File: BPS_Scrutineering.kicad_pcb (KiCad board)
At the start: 2 copper layers, 89 x 172 mm, 158 parts, among them J1 Conn_01x09, J10 BottomConn, J2 Conn_01x09, J3 Conn_01x09, J4 Conn_01x09, J5 TopConn, J6 BottomConn, J7 TopConn, J8 BottomConn, J9 TopConn, SW1 SW_DIP_x07, SW2 SW_DIP_x07, SW3 SW_DIP_x07, SW4 SW_DIP_x07, SW5 SW_DIP_x07, SW6 SW_DIP_x07

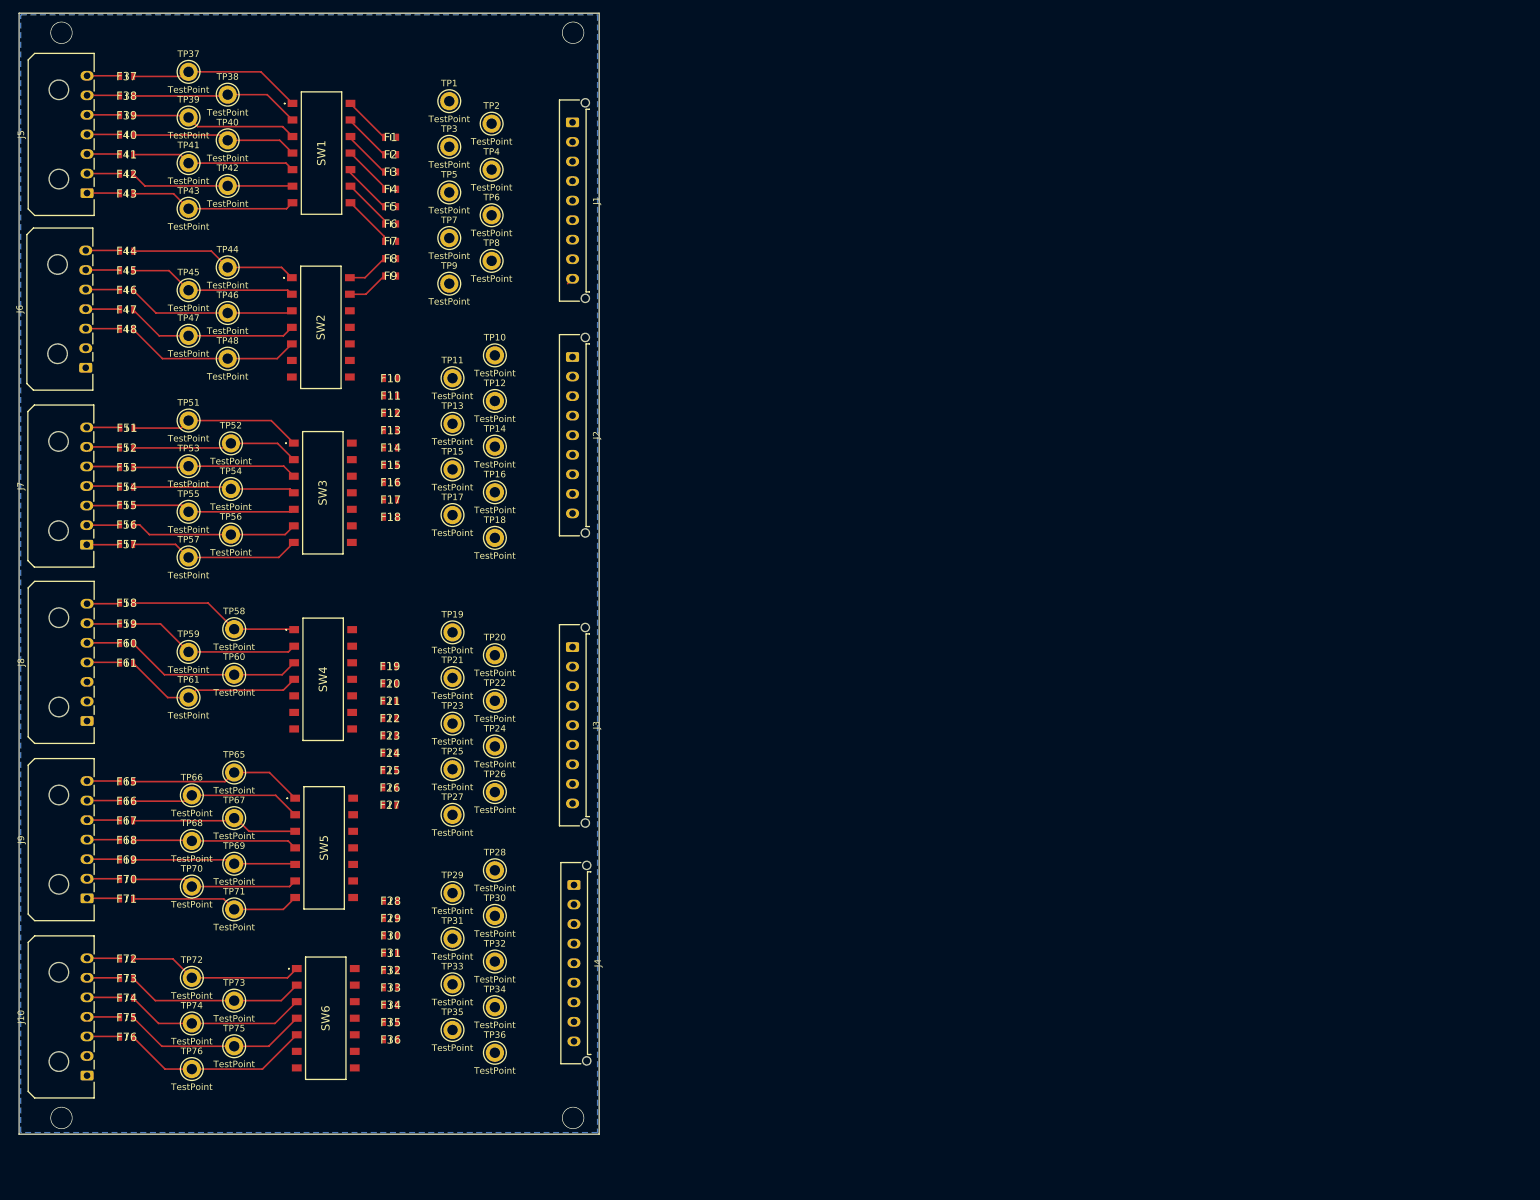
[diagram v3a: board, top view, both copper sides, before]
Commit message: fixed spacing and schematic
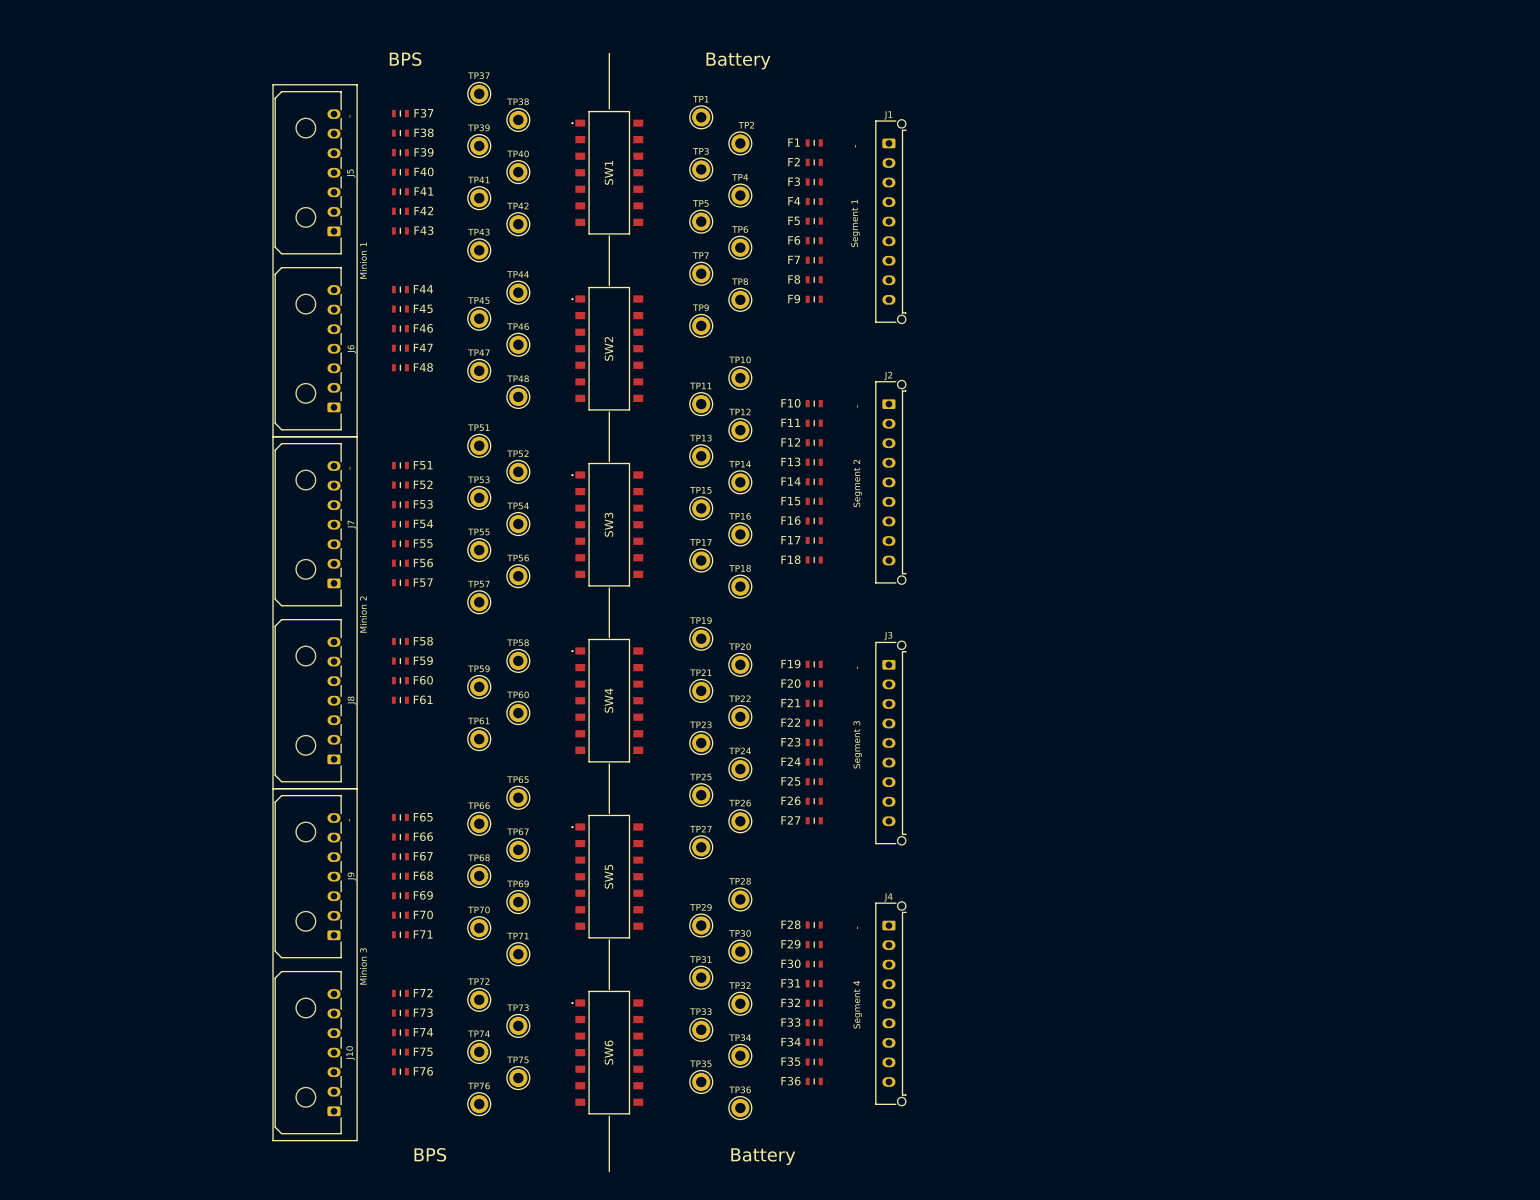
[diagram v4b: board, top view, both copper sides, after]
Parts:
- moved F18 65.3 mm to (142.0, 97.8)
- moved F36 65.3 mm to (142.0, 177.8)
- moved F17 65.3 mm to (142.0, 94.8)
- moved F35 65.3 mm to (142.0, 174.8)
- moved F16 65.3 mm to (142.0, 91.8)
- moved F34 65.3 mm to (142.0, 171.8)
- moved F15 65.2 mm to (142.0, 88.8)
- moved F33 65.2 mm to (142.0, 168.8)
- moved F14 65.2 mm to (142.0, 85.8)
- moved F32 65.2 mm to (142.0, 165.8)
- moved F13 65.2 mm to (142.0, 82.8)
- moved F31 65.2 mm to (142.0, 162.8)
- moved F27 65.2 mm to (142.0, 137.8)
- moved F12 65.2 mm to (142.0, 79.8)
- moved F26 65.1 mm to (142.0, 134.8)
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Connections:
- TP1 pad 1: Net-(J1-Pin_1) -> /1-_BATT
- TP10 pad 1: Net-(J2-Pin_1) -> /9-_BATT
- TP11 pad 1: Net-(J2-Pin_2) -> /9+_BATT
- TP12 pad 1: Net-(J2-Pin_3) -> /10+_BATT
- TP13 pad 1: Net-(J2-Pin_4) -> /11+_BATT
- TP14 pad 1: Net-(J2-Pin_5) -> /12+_BATT
- TP15 pad 1: Net-(J2-Pin_6) -> /13+_BATT
- TP16 pad 1: Net-(J2-Pin_7) -> /14+_BATT
- TP17 pad 1: Net-(J2-Pin_8) -> /15+_BATT
- TP18 pad 1: Net-(J2-Pin_9) -> /16+_BATT
- TP19 pad 1: Net-(J3-Pin_1) -> /17-_BATT
- TP2 pad 1: Net-(J1-Pin_2) -> /1+_BATT
- TP20 pad 1: Net-(J3-Pin_2) -> /17+_BATT
- TP21 pad 1: Net-(J3-Pin_3) -> /18+_BATT
- TP22 pad 1: Net-(J3-Pin_4) -> /19+_BATT
- TP23 pad 1: Net-(J3-Pin_5) -> /20+_BATT
- TP24 pad 1: Net-(J3-Pin_6) -> /21+_BATT
- TP25 pad 1: Net-(J3-Pin_7) -> /22+_BATT
- TP26 pad 1: Net-(J3-Pin_8) -> /23+_BATT
- TP27 pad 1: Net-(J3-Pin_9) -> /24+_BATT
- TP28 pad 1: Net-(J4-Pin_1) -> /25-_BATT
- TP29 pad 1: Net-(J4-Pin_2) -> /25+_BATT
- TP3 pad 1: Net-(J1-Pin_3) -> /2+_BATT
- TP30 pad 1: Net-(J4-Pin_3) -> /26+_BATT
- TP31 pad 1: Net-(J4-Pin_4) -> /27+_BATT
- TP32 pad 1: Net-(J4-Pin_5) -> /28+_BATT
- TP33 pad 1: Net-(J4-Pin_6) -> /29+_BATT
- TP34 pad 1: Net-(J4-Pin_7) -> /30+_BATT
- TP35 pad 1: Net-(J4-Pin_8) -> /31+_BATT
- TP36 pad 1: Net-(J4-Pin_9) -> /32+_BATT
- TP4 pad 1: Net-(J1-Pin_4) -> /3+_BATT
- TP5 pad 1: Net-(J1-Pin_5) -> /4+_BATT
- TP6 pad 1: Net-(J1-Pin_6) -> /5+_BATT
- TP7 pad 1: Net-(J1-Pin_7) -> /6+_BATT
- TP8 pad 1: Net-(J1-Pin_8) -> /7+_BATT
- TP9 pad 1: Net-(J1-Pin_9) -> /8+_BATT
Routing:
- net /BPS_MINION_3/Minion_Out_12: track 29.3 -> 0.00 mm
- net /BPS_MINION_3/Minion_Out_11: track 28.7 -> 0.00 mm
- net /BPS_MINION_3/Minion_Out_10: track 28.1 -> 0.00 mm
- net /BPS_MINION_2/Minion_Out_11: track 28.1 -> 0.00 mm
- net /BPS_MINION_3/Minion_Out_9: track 27.5 -> 0.00 mm
- net /BPS_MINION_2/Minion_Out_10: track 27.5 -> 0.00 mm
- net /BPS_MINION_1/Minion_Out_12: track 27.2 -> 0.00 mm
- net /BPS_MINION_3/Minion_Out_1: track 27.1 -> 0.00 mm
- net /BPS_MINION_3/Minion_Out_8: track 26.9 -> 0.00 mm
- net /BPS_MINION_2/Minion_Out_9: track 26.8 -> 0.00 mm
- net /BPS_MINION_1/Minion_Out_1: track 26.7 -> 0.00 mm
- net /BPS_MINION_1/Minion_Out_11: track 26.5 -> 0.00 mm
- net /BPS_MINION_2/Minion_Out_1: track 26.5 -> 0.00 mm
- net /BPS_MINION_3/Minion_Out_2: track 26.5 -> 0.00 mm
- net /BPS_MINION_2/Minion_Out_7: track 26.4 -> 0.00 mm
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- removed copper zone on B.Cu, net (none)
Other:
- board outline removed
- board text added: "-"
- board text added: "BPS"
- board text added: "Battery"
- board text added: "Minion 1"
- board text added: "Minion 2"
- board text added: "Minion 3"
- board text added: "Segment 1"
- board text added: "Segment 2"
- board text added: "Segment 3"
- board text added: "Segment 4"

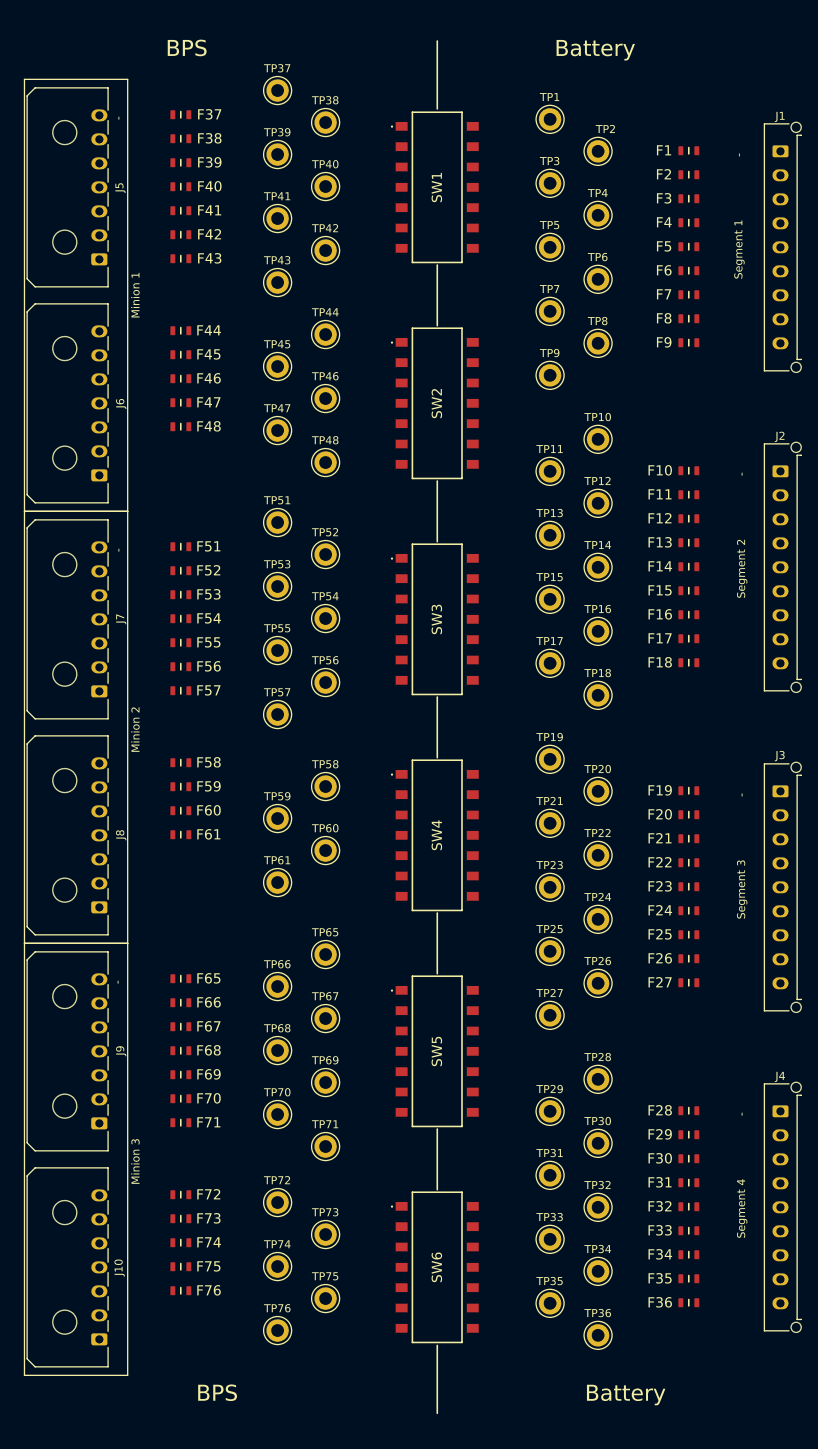
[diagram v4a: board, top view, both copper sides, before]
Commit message: Added traces and edge cuts
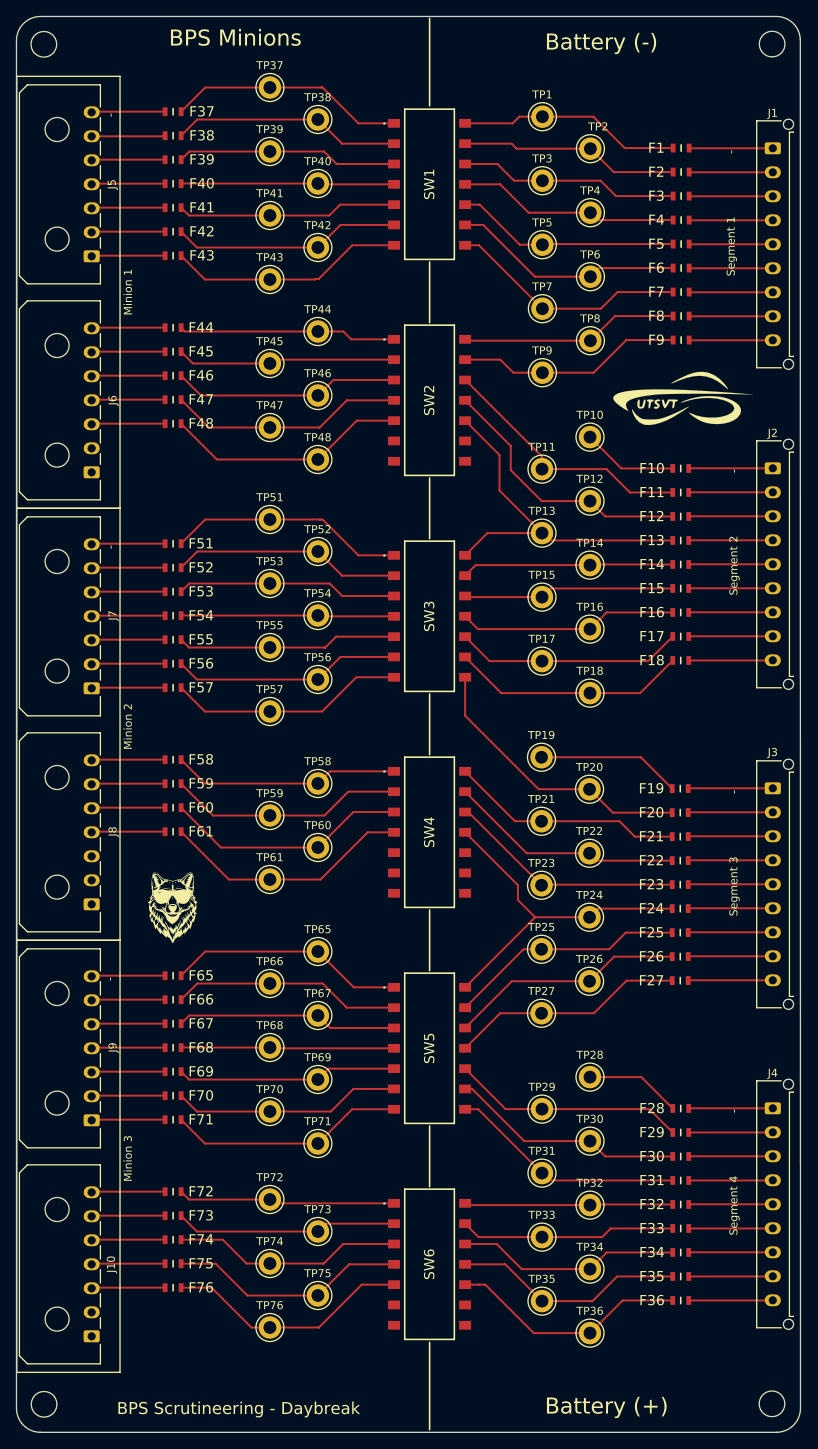
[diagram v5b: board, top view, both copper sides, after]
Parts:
- added G***: LOGO, UTSVT_Special:UTSVT_Logo_Symbol, F.Cu at (141.0, 64.9)
- added G***: LOGO, footprints:wolf front, F.Cu at (77.5, 128.4)
- added G***: LOGO, UTSVT_Special:Hallock_Image, B.Cu at (108.2, 100.0)
- added REF**: MountingHole_3.2mm_M3, MountingHole:MountingHole_3.2mm_M3, F.Cu at (61.4, 20.5)
- added REF**: MountingHole_3.2mm_M3, MountingHole:MountingHole_3.2mm_M3, F.Cu at (152.4, 190.4)
- added REF**: MountingHole_3.2mm_M3, MountingHole:MountingHole_3.2mm_M3, F.Cu at (61.5, 190.5)
- added REF**: MountingHole_3.2mm_M3, MountingHole:MountingHole_3.2mm_M3, F.Cu at (152.5, 20.5)
- moved F24 1.10 mm to (141.0, 128.5)
- moved F25 1.10 mm to (141.0, 131.5)
- moved F26 1.10 mm to (141.0, 134.5)
- moved F27 1.10 mm to (141.0, 137.5)
- moved F19 1.10 mm to (141.0, 113.5)
- moved F20 1.10 mm to (141.0, 116.5)
- moved F21 1.10 mm to (141.0, 119.5)
- moved F22 1.10 mm to (141.0, 122.5)
- moved F23 1.10 mm to (141.0, 125.5)
- moved TP19 1.10 mm to (123.6, 109.6)
- moved TP21 1.10 mm to (123.6, 117.6)
- moved TP23 1.10 mm to (123.6, 125.6)
- moved TP25 1.10 mm to (123.6, 133.6)
- moved TP27 1.10 mm to (123.6, 141.6)
- moved TP20 1.10 mm to (129.6, 113.6)
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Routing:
- net /11+_BATT: track 0.00 -> 45.5 mm
- net /21+_BATT: track 0.00 -> 44.2 mm
- net /17+_BATT: track 0.00 -> 35.7 mm
- net /10+_BATT: track 0.00 -> 33.7 mm
- net /9+_BATT: track 0.00 -> 32.7 mm
- net /BPS_MINION_2/Minion_Out_11: track 0.00 -> 31.5 mm
- net /BPS_MINION_3/Minion_Out_12: track 0.00 -> 30.9 mm
- net /BPS_MINION_2/Minion_Out_10: track 0.00 -> 30.5 mm
- net /BPS_MINION_1/Minion_Out_12: track 0.00 -> 30.5 mm
- net /6+_BATT: track 0.00 -> 30.4 mm
- net /32+_BATT: track 0.00 -> 30.2 mm
- net /BPS_MINION_3/Minion_Out_11: track 0.00 -> 29.9 mm
- net /22+_BATT: track 0.00 -> 29.8 mm
- net /BPS_MINION_1/Minion_Out_1: track 0.00 -> 29.8 mm
- net /20+_BATT: track 0.00 -> 29.7 mm
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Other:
- board outline added: 98 x 177 mm
- board text added: "BPS Minions"
- board text added: "BPS Scrutineering - Daybreak"
- board text added: "Battery (+)"
- board text added: "Battery (-)"
- board text removed: "BPS"
- board text removed: "Battery"
